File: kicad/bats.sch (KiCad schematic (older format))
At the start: 12 parts

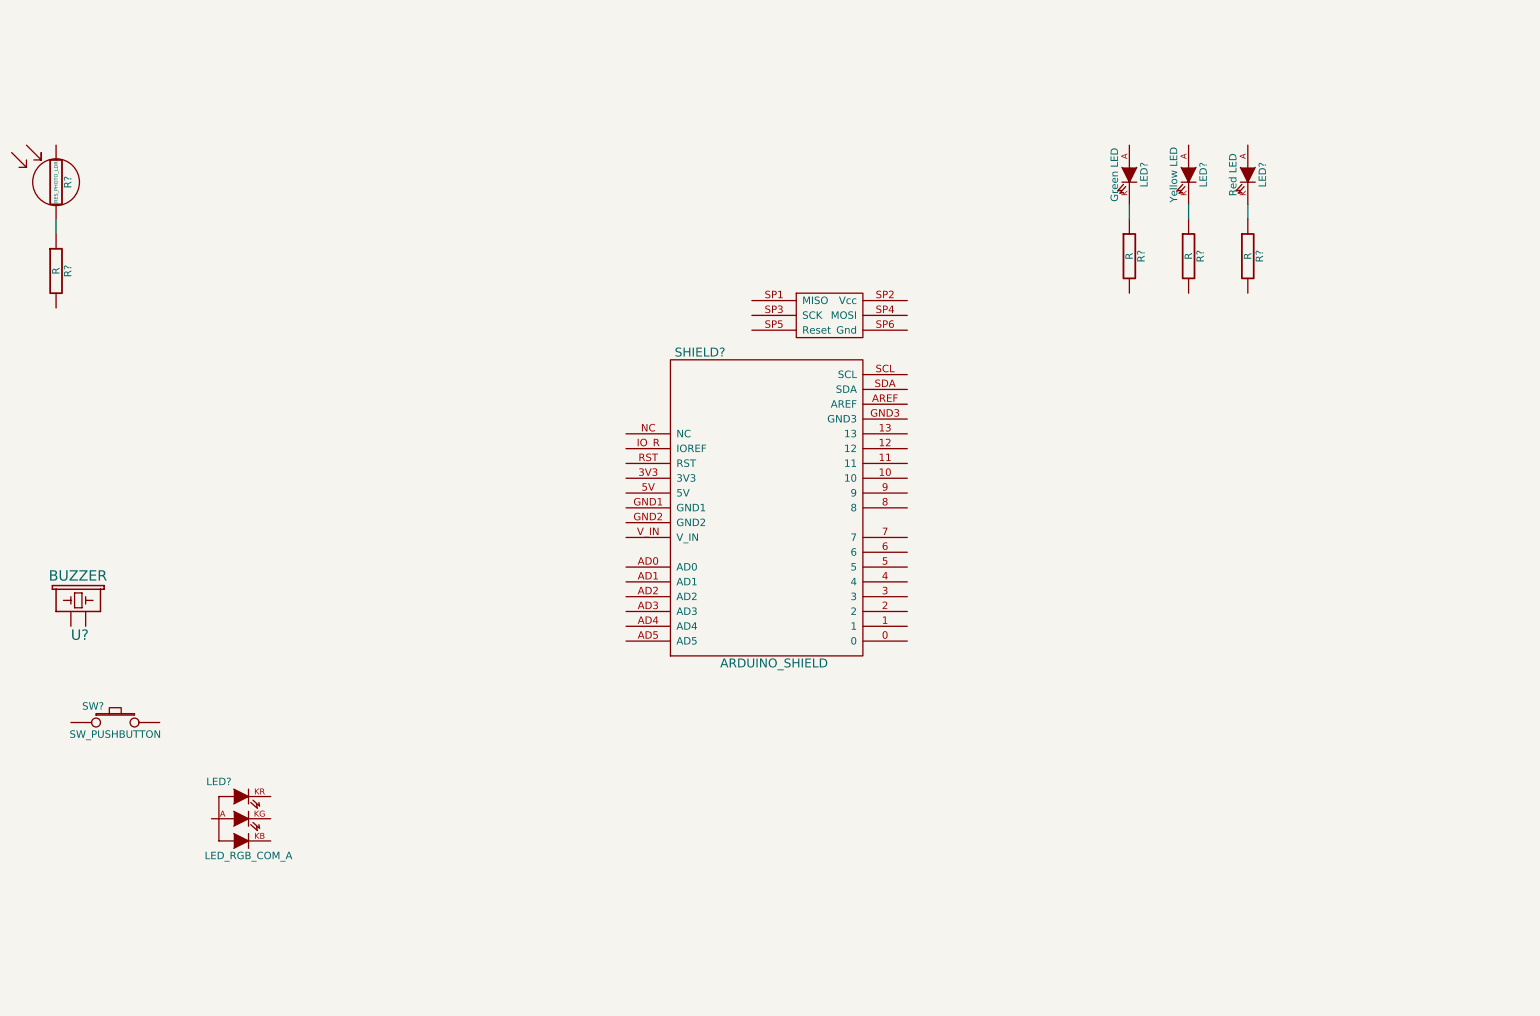
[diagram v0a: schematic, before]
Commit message: Mais avances no esquema do circuito
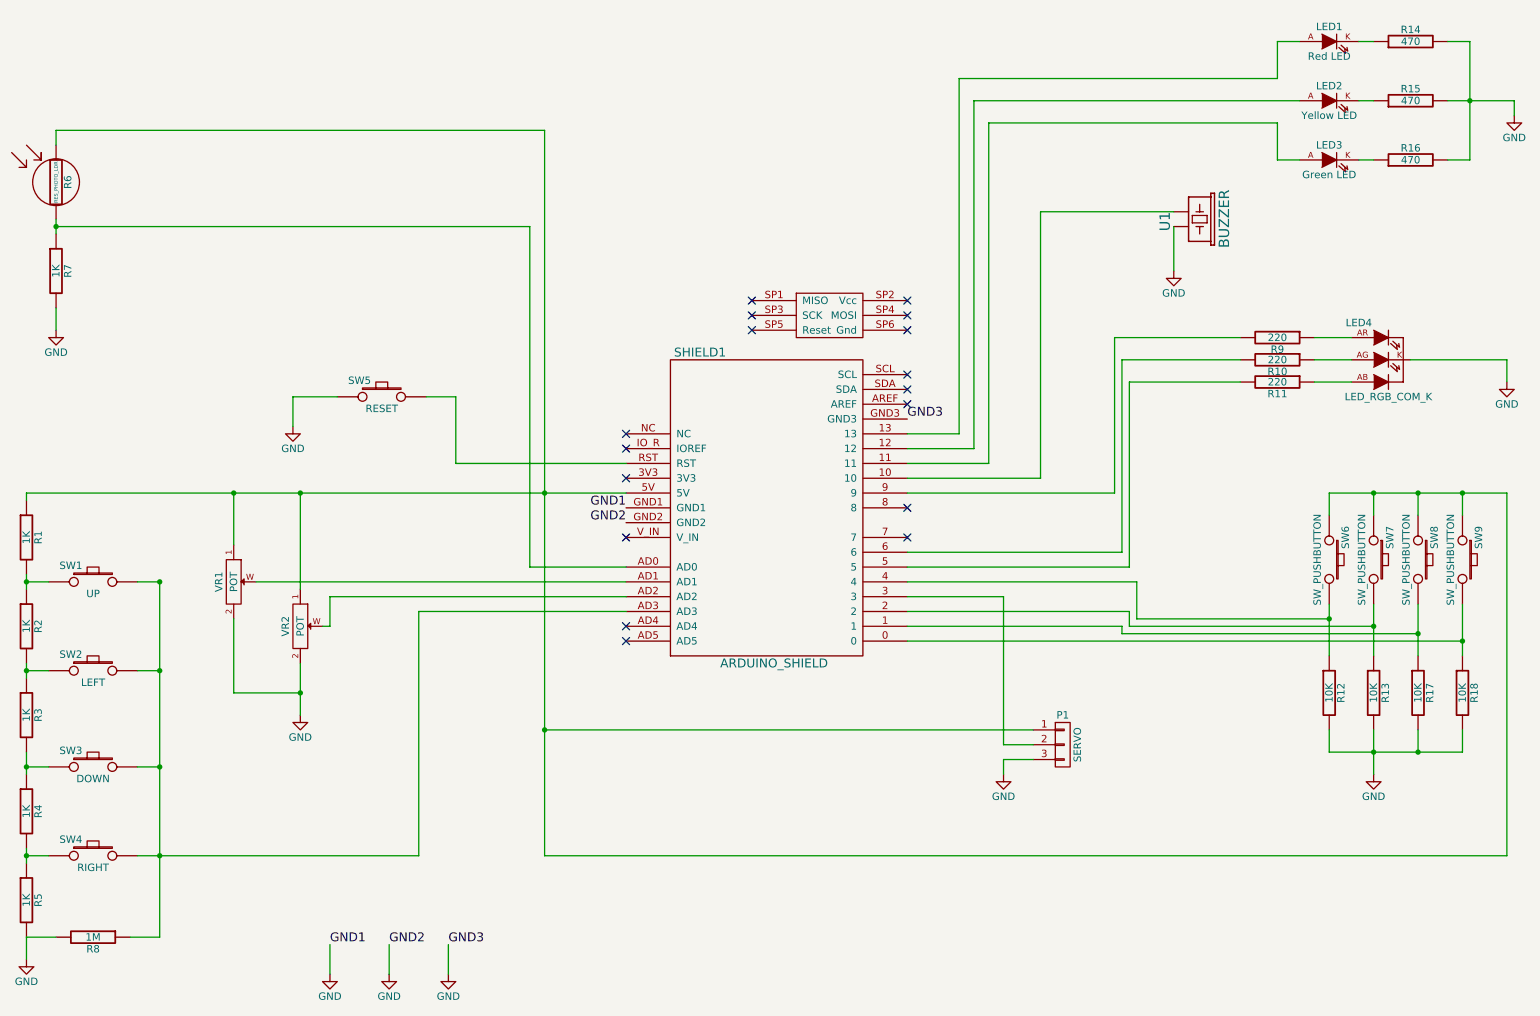
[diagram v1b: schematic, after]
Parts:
- removed LED?: LED_RGB_COM_A, symbol LED_RGB_COM_A
- added LED4: LED_RGB_COM_K, FT:LED_CUBE_BASE_4PIN, symbol LED_RGB_COM_K
- added P1: SERVO, FT:1X03, symbol CONN_01X03
- added R1, R2, R3, R4, R5: 1K, Resistors_ThroughHole:Resistor_Horizontal_RM10mm, symbol R
- added R10, R11, R9: 220, Resistors_ThroughHole:Resistor_Horizontal_RM10mm, symbol R
- added R12, R13, R17, R18: 10K, Resistors_ThroughHole:Resistor_Horizontal_RM10mm, symbol R
- added R8: 1M, Resistors_ThroughHole:Resistor_Horizontal_RM10mm, symbol R
- added SW1: UP, FT:SW_PUSHBUTTON_PTH, symbol SW_PUSHBUTTON
- added SW2: LEFT, FT:SW_PUSHBUTTON_PTH, symbol SW_PUSHBUTTON
- added SW3: DOWN, FT:SW_PUSHBUTTON_PTH, symbol SW_PUSHBUTTON
- added SW4: RIGHT, FT:SW_PUSHBUTTON_PTH, symbol SW_PUSHBUTTON
- added SW5: RESET, FT:SW_PUSHBUTTON_PTH, symbol SW_PUSHBUTTON
- added SW7, SW8: SW_PUSHBUTTON, FT:SW_PUSHBUTTON_PTH, symbol SW_PUSHBUTTON
- added SW9: SW_PUSHBUTTON, Buttons_Switches_ThroughHole:SW_PUSH, symbol SW_PUSHBUTTON
- added VR1, VR2: POT, Potentiometers:Potentiometer_Alps-RK16-single, symbol POT
- LED1, LED2, LED3: renamed from LED?; footprint (none) -> FT:LED-3MM
- R14, R15, R16: renamed from R?; value R -> 470; footprint (none) -> Resistors_ThroughHole:Resistor_Horizontal_RM10mm
- R6: renamed from R?; footprint (none) -> Resistors_ThroughHole:Resistor_Horizontal_RM10mm
- R7: renamed from R?; value R -> 1K; footprint (none) -> Resistors_ThroughHole:Resistor_Horizontal_RM10mm
- SW6: renamed from SW?; footprint (none) -> FT:SW_PUSHBUTTON_PTH
- U1: renamed from U?; footprint (none) -> Buzzers_Beepers:MagneticBuzzer_StarMicronics_HMB-06_HMB-12
- gave numbers to parts that had none: 1
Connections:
- net at SHIELD1.0: now also R18.1, SW9.2
- net at SHIELD1.1: now also R17.1, SW8.2
- net at SHIELD1.10: now also U1.2 (GND)
- net at SHIELD1.11: now also LED3.A
- net at SHIELD1.12: now also LED2.A
- net at SHIELD1.13: now also LED1.A
- net at SHIELD1.2: now also R13.1, SW7.2
- net at SHIELD1.3: now also P1.2 (P2)
- net at SHIELD1.4: now also SW6.2, R12.1
- net at SHIELD1.5: now also R11.2
- net at SHIELD1.5V: now also R6.1, SW6.1, P1.1 (P1), R1.1, SW7.1, SW8.1, SW9.1, VR1.1, VR2.1
- net at SHIELD1.6: now also R10.2
- net at SHIELD1.9: now also R9.2
- net at SHIELD1.AD0: now also R6.2, R7.1
- net at SHIELD1.AD1: now also VR1.W
- net at SHIELD1.AD2: now also VR2.W
- net at SHIELD1.AD3: now also R8.1, SW1.2, SW2.2, SW3.2, SW4.2
- net GND: now reaches SHIELD1.GND1
- net GND: now also R14.2, R15.2, R16.2, R7.2, SHIELD1.GND2, SHIELD1.GND3, U1.1 (POS), LED4.K, P1.3 (P3), R12.2, R13.2, R17.2, R18.2, R5.2, R8.2, SW5.1, VR1.2, VR2.2
- net at SHIELD1.RST: now also SW5.2
- new net: LED4.AB, R11.1
- new net: LED4.AG, R10.1
- new net: LED4.AR, R9.1
- new net: R1.2, R2.1, SW1.1
- new net: R2.2, R3.1, SW2.1
- new net: R3.2, R4.1, SW3.1
- new net: R4.2, R5.1, SW4.1
- no-connect marks 0 -> 17
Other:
- moved on the sheet: LED1, LED2, LED3, R14, R15, R16, SW6, U1

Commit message: Engadido o esquema en formato pdf
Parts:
- SW6: value SW_PUSHBUTTON -> UP
- SW7: value SW_PUSHBUTTON -> LEFT
- SW8: value SW_PUSHBUTTON -> DOWN
- SW9: value SW_PUSHBUTTON -> RIGHT
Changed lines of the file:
@@
 P 9600 4300
 F 0 "SW6" H 9450 4410 50  0000 C CNN
-F 1 "SW_PUSHBUTTON" H 9600 4220 50  0000 C CNN
+F 1 "UP" H 9600 4220 50  0000 C CNN
 F 2 "FT:SW_PUSHBUTTON_PTH" H 9600 4300 60  0001 C CNN
 F 3 "" H 9600 4300 60  0000 C CNN
@@
 P 9900 4300
 F 0 "SW7" H 9750 4410 50  0000 C CNN
-F 1 "SW_PUSHBUTTON" H 9900 4220 50  0000 C CNN
+F 1 "LEFT" H 9900 4220 50  0000 C CNN
 F 2 "FT:SW_PUSHBUTTON_PTH" H 9900 4300 60  0001 C CNN
 F 3 "" H 9900 4300 60  0000 C CNN
@@
 P 10200 4300
 F 0 "SW8" H 10050 4410 50  0000 C CNN
-F 1 "SW_PUSHBUTTON" H 10200 4220 50  0000 C CNN
+F 1 "DOWN" H 10200 4220 50  0000 C CNN
 F 2 "FT:SW_PUSHBUTTON_PTH" H 10200 4300 60  0001 C CNN
 F 3 "" H 10200 4300 60  0000 C CNN
@@
 P 10500 4300
 F 0 "SW9" H 10350 4410 50  0000 C CNN
-F 1 "SW_PUSHBUTTON" H 10500 4220 50  0000 C CNN
+F 1 "RIGHT" H 10500 4220 50  0000 C CNN
 F 2 "Buttons_Switches_ThroughHole:SW_PUSH" H 10500 4300 60  0001 C CNN
 F 3 "" H 10500 4300 60  0000 C CNN
@@
 	9900 800  9800 800
 Wire Wire Line
-	1000 2000 1000 2100
+	1000 2000 1000 2050
+Wire Wire Line
+	1000 2050 1000 2100
 Wire Wire Line
 	10550 1600 10400 1600
 Wire Wire Line
-	10550 800  10550 1600
+	10550 800  10550 1200
+Wire Wire Line
+	10550 1200 10550 1600
 Wire Wire Line
 	10550 800  10400 800
 Wire Wire Line
-	10400 1200 10850 1200
+	10400 1200 10550 1200
+Wire Wire Line
+	10550 1200 10850 1200
 Connection ~ 10550 1200
 Wire Wire Line
@@
 Connection ~ 1000 2050
 Wire Wire Line
-	800  3850 4850 3850
-Wire Wire Line
-	4300 1400 4300 6300
+	800  3850 2200 3850
+Wire Wire Line
+	2200 3850 2650 3850
+Wire Wire Line
+	2650 3850 4300 3850
+Wire Wire Line
+	4300 3850 4850 3850
+Wire Wire Line
+	4300 1400 4300 3850
+Wire Wire Line
+	4300 3850 4300 5450
+Wire Wire Line
+	4300 5450 4300 6300
 Wire Wire Line
 	4300 1400 1000 1400
@@
 	8550 2050 8550 2350
 Wire Wire Line
-	9600 4600 9600 4950
-Wire Wire Line
-	9900 4600 9900 4950
-Wire Wire Line
-	10200 4600 10200 4950
-Wire Wire Line
-	10500 4600 10500 4950
+	9600 4600 9600 4700
+Wire Wire Line
+	9600 4700 9600 4950
+Wire Wire Line
+	9900 4600 9900 4750
+Wire Wire Line
+	9900 4750 9900 4950
+Wire Wire Line
+	10200 4600 10200 4800
+Wire Wire Line
+	10200 4800 10200 4950
+Wire Wire Line
+	10500 4600 10500 4850
+Wire Wire Line
+	10500 4850 10500 4950
 Wire Wire Line
 	9900 3850 9900 4000
@@
 Connection ~ 10500 3850
 Wire Wire Line
-	9600 3850 10800 3850
+	9600 3850 9900 3850
+Wire Wire Line
+	9900 3850 10200 3850
+Wire Wire Line
+	10200 3850 10500 3850
+Wire Wire Line
+	10500 3850 10800 3850
 Wire Wire Line
 	9600 3850 9600 4000
@@
 	9600 5450 9600 5600
 Wire Wire Line
-	9600 5600 10500 5600
+	9600 5600 9900 5600
+Wire Wire Line
+	9900 5600 10200 5600
+Wire Wire Line
+	10200 5600 10500 5600
 Wire Wire Line
 	10500 5600 10500 5450
 Wire Wire Line
-	9900 5450 9900 5750
+	9900 5450 9900 5600
+Wire Wire Line
+	9900 5600 9900 5750
 Connection ~ 9900 5600
 Wire Wire Line
@@
 	7400 5650 7400 5750
 Wire Wire Line
-	1700 4450 1700 6850
+	1700 4450 1700 5050
+Wire Wire Line
+	1700 5050 1700 5700
+Wire Wire Line
+	1700 5700 1700 6300
+Wire Wire Line
+	1700 6300 1700 6850
 Wire Wire Line
 	1550 5700 1700 5700
@@
 Connection ~ 1700 5050
 Wire Wire Line
-	800  4400 800  4500
+	800  4400 800  4450
+Wire Wire Line
+	800  4450 800  4500
 Wire Wire Line
 	950  4450 800  4450
 Connection ~ 800  4450
 Wire Wire Line
-	800  5000 800  5100
+	800  5000 800  5050
+Wire Wire Line
+	800  5050 800  5100
 Wire Wire Line
 	950  5050 800  5050
 Connection ~ 800  5050
 Wire Wire Line
-	800  5600 800  5750
+	800  5600 800  5700
+Wire Wire Line
+	800  5700 800  5750
 Wire Wire Line
 	950  5700 800  5700
 Connection ~ 800  5700
 Wire Wire Line
-	800  6250 800  6350
+	800  6250 800  6300
+Wire Wire Line
+	800  6300 800  6350
 Wire Wire Line
 	950  6300 800  6300
@@
 	1700 6850 1500 6850
 Wire Wire Line
-	1550 6300 3450 6300
+	1550 6300 1700 6300
+Wire Wire Line
+	1700 6300 3450 6300
 Connection ~ 1700 6300
 Wire Wire Line
@@
 	2200 5200 2650 5200
 Wire Wire Line
-	2650 5000 2650 5350
+	2650 5000 2650 5200
+Wire Wire Line
+	2650 5200 2650 5350
 Connection ~ 2650 5200
 Wire Wire Line

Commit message: A PCB empeza a coller forma.
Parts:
- LED4: footprint FT:LED_CUBE_BASE_4PIN -> FT:LED-RGB-8MM-COM-K-MINIMAL
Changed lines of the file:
@@
 F 0 "LED4" H 9800 2900 50  0000 C CNN
 F 1 "LED_RGB_COM_K" H 10000 2400 50  0000 C CNN
-F 2 "FT:LED_CUBE_BASE_4PIN" H 9950 2800 60  0001 C CNN
+F 2 "FT:LED-RGB-8MM-COM-K-MINIMAL" H 9950 2800 60  0001 C CNN
 F 3 "" H 9950 2800 60  0000 C CNN
 	1    9950 2800
@@
 	9900 800  9800 800
 Wire Wire Line
-	1000 2000 1000 2050
-Wire Wire Line
-	1000 2050 1000 2100
+	1000 2000 1000 2100
 Wire Wire Line
 	10550 1600 10400 1600
 Wire Wire Line
-	10550 800  10550 1200
-Wire Wire Line
-	10550 1200 10550 1600
+	10550 800  10550 1600
 Wire Wire Line
 	10550 800  10400 800
 Wire Wire Line
-	10400 1200 10550 1200
-Wire Wire Line
-	10550 1200 10850 1200
+	10400 1200 10850 1200
 Connection ~ 10550 1200
 Wire Wire Line
@@
 Connection ~ 1000 2050
 Wire Wire Line
-	800  3850 2200 3850
-Wire Wire Line
-	2200 3850 2650 3850
-Wire Wire Line
-	2650 3850 4300 3850
-Wire Wire Line
-	4300 3850 4850 3850
-Wire Wire Line
-	4300 1400 4300 3850
-Wire Wire Line
-	4300 3850 4300 5450
-Wire Wire Line
-	4300 5450 4300 6300
+	800  3850 4850 3850
+Wire Wire Line
+	4300 1400 4300 6300
 Wire Wire Line
 	4300 1400 1000 1400
@@
 	8550 2050 8550 2350
 Wire Wire Line
-	9600 4600 9600 4700
-Wire Wire Line
-	9600 4700 9600 4950
-Wire Wire Line
-	9900 4600 9900 4750
-Wire Wire Line
-	9900 4750 9900 4950
-Wire Wire Line
-	10200 4600 10200 4800
-Wire Wire Line
-	10200 4800 10200 4950
-Wire Wire Line
-	10500 4600 10500 4850
-Wire Wire Line
-	10500 4850 10500 4950
+	9600 4600 9600 4950
+Wire Wire Line
+	9900 4600 9900 4950
+Wire Wire Line
+	10200 4600 10200 4950
+Wire Wire Line
+	10500 4600 10500 4950
 Wire Wire Line
 	9900 3850 9900 4000
@@
 Connection ~ 10500 3850
 Wire Wire Line
-	9600 3850 9900 3850
-Wire Wire Line
-	9900 3850 10200 3850
-Wire Wire Line
-	10200 3850 10500 3850
-Wire Wire Line
-	10500 3850 10800 3850
+	9600 3850 10800 3850
 Wire Wire Line
 	9600 3850 9600 4000
@@
 	9600 5450 9600 5600
 Wire Wire Line
-	9600 5600 9900 5600
-Wire Wire Line
-	9900 5600 10200 5600
-Wire Wire Line
-	10200 5600 10500 5600
+	9600 5600 10500 5600
 Wire Wire Line
 	10500 5600 10500 5450
 Wire Wire Line
-	9900 5450 9900 5600
-Wire Wire Line
-	9900 5600 9900 5750
+	9900 5450 9900 5750
 Connection ~ 9900 5600
 Wire Wire Line
@@
 	7400 5650 7400 5750
 Wire Wire Line
-	1700 4450 1700 5050
-Wire Wire Line
-	1700 5050 1700 5700
-Wire Wire Line
-	1700 5700 1700 6300
-Wire Wire Line
-	1700 6300 1700 6850
+	1700 4450 1700 6850
 Wire Wire Line
 	1550 5700 1700 5700
@@
 Connection ~ 1700 5050
 Wire Wire Line
-	800  4400 800  4450
-Wire Wire Line
-	800  4450 800  4500
+	800  4400 800  4500
 Wire Wire Line
 	950  4450 800  4450
 Connection ~ 800  4450
 Wire Wire Line
-	800  5000 800  5050
-Wire Wire Line
-	800  5050 800  5100
+	800  5000 800  5100
 Wire Wire Line
 	950  5050 800  5050
 Connection ~ 800  5050
 Wire Wire Line
-	800  5600 800  5700
-Wire Wire Line
-	800  5700 800  5750
+	800  5600 800  5750
 Wire Wire Line
 	950  5700 800  5700
 Connection ~ 800  5700
 Wire Wire Line
-	800  6250 800  6300
-Wire Wire Line
-	800  6300 800  6350
+	800  6250 800  6350
 Wire Wire Line
 	950  6300 800  6300
@@
 	1700 6850 1500 6850
 Wire Wire Line
-	1550 6300 1700 6300
-Wire Wire Line
-	1700 6300 3450 6300
+	1550 6300 3450 6300
 Connection ~ 1700 6300
 Wire Wire Line
@@
 	2200 5200 2650 5200
 Wire Wire Line
-	2650 5000 2650 5200
-Wire Wire Line
-	2650 5200 2650 5350
+	2650 5000 2650 5350
 Connection ~ 2650 5200
 Wire Wire Line

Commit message: Mais cambios non especificados, facemos o commit antes de borrar o conxunto de pulsadores analóxicos.
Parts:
- SW9: footprint Buttons_Switches_ThroughHole:SW_PUSH -> FT:SW_PUSHBUTTON_PTH
- VR1, VR2: footprint Potentiometers:Potentiometer_Alps-RK16-single -> (none)
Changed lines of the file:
@@
 $EndComp
 $Comp
-L GND #PWR01
+L GND #PWR2
 U 1 1 558AD005
 P 1000 2750
-F 0 "#PWR01" H 1000 2500 50  0001 C CNN
+F 0 "#PWR2" H 1000 2500 50  0001 C CNN
 F 1 "GND" H 1000 2600 50  0000 C CNN
 F 2 "" H 1000 2750 60  0000 C CNN
@@
 $EndComp
 $Comp
-L GND #PWR02
+L GND #PWR9
 U 1 1 558AE0E5
 P 8550 2350
-F 0 "#PWR02" H 8550 2100 50  0001 C CNN
+F 0 "#PWR9" H 8550 2100 50  0001 C CNN
 F 1 "GND" H 8550 2200 50  0000 C CNN
 F 2 "" H 8550 2350 60  0000 C CNN
@@
 F 0 "SW9" H 10350 4410 50  0000 C CNN
 F 1 "RIGHT" H 10500 4220 50  0000 C CNN
-F 2 "Buttons_Switches_ThroughHole:SW_PUSH" H 10500 4300 60  0001 C CNN
+F 2 "FT:SW_PUSHBUTTON_PTH" H 10500 4300 60  0001 C CNN
 F 3 "" H 10500 4300 60  0000 C CNN
 	1    10500 4300
@@
 $EndComp
 $Comp
-L GND #PWR03
+L GND #PWR10
 U 1 1 558AF401
 P 9900 5750
-F 0 "#PWR03" H 9900 5500 50  0001 C CNN
+F 0 "#PWR10" H 9900 5500 50  0001 C CNN
 F 1 "GND" H 9900 5600 50  0000 C CNN
 F 2 "" H 9900 5750 60  0000 C CNN
@@
 $EndComp
 $Comp
-L GND #PWR04
+L GND #PWR11
 U 1 1 558B19E1
 P 10800 3100
-F 0 "#PWR04" H 10800 2850 50  0001 C CNN
+F 0 "#PWR11" H 10800 2850 50  0001 C CNN
 F 1 "GND" H 10800 2950 50  0000 C CNN
 F 2 "" H 10800 3100 60  0000 C CNN
@@
 $EndComp
 $Comp
-L GND #PWR05
+L GND #PWR8
 U 1 1 558B2CF4
 P 7400 5750
-F 0 "#PWR05" H 7400 5500 50  0001 C CNN
+F 0 "#PWR8" H 7400 5500 50  0001 C CNN
 F 1 "GND" H 7400 5600 50  0000 C CNN
 F 2 "" H 7400 5750 60  0000 C CNN
@@
 $EndComp
 $Comp
-L GND #PWR06
+L GND #PWR1
 U 1 1 558B5809
 P 800 7000
-F 0 "#PWR06" H 800 6750 50  0001 C CNN
+F 0 "#PWR1" H 800 6750 50  0001 C CNN
 F 1 "GND" H 800 6850 50  0000 C CNN
 F 2 "" H 800 7000 60  0000 C CNN
@@
 $EndComp
 $Comp
-L POT VR1
-U 1 1 558B64D3
-P 2200 4450
-F 0 "VR1" H 2200 4350 50  0000 C CNN
-F 1 "POT" H 2200 4450 50  0000 C CNN
-F 2 "Potentiometers:Potentiometer_Alps-RK16-single" H 2200 4450 60  0001 C CNN
-F 3 "" H 2200 4450 60  0000 C CNN
-	1    2200 4450
-	0    1    1    0
-$EndComp
-$Comp
-L POT VR2
-U 1 1 558B673E
-P 2650 4750
-F 0 "VR2" H 2650 4650 50  0000 C CNN
-F 1 "POT" H 2650 4750 50  0000 C CNN
-F 2 "Potentiometers:Potentiometer_Alps-RK16-single" H 2650 4750 60  0001 C CNN
-F 3 "" H 2650 4750 60  0000 C CNN
-	1    2650 4750
-	0    1    1    0
-$EndComp
-$Comp
-L GND #PWR07
+L GND #PWR4
 U 1 1 558B6A63
 P 2650 5350
-F 0 "#PWR07" H 2650 5100 50  0001 C CNN
+F 0 "#PWR4" H 2650 5100 50  0001 C CNN
 F 1 "GND" H 2650 5200 50  0000 C CNN
 F 2 "" H 2650 5350 60  0000 C CNN
@@
 $EndComp
 $Comp
-L GND #PWR08
+L GND #PWR3
 U 1 1 558B7665
 P 2600 3400
-F 0 "#PWR08" H 2600 3150 50  0001 C CNN
+F 0 "#PWR3" H 2600 3150 50  0001 C CNN
 F 1 "GND" H 2600 3250 50  0000 C CNN
 F 2 "" H 2600 3400 60  0000 C CNN
@@
 	2600 3200 2600 3400
 $Comp
-L GND #PWR09
+L GND #PWR12
 U 1 1 558C0B72
 P 10850 1300
-F 0 "#PWR09" H 10850 1050 50  0001 C CNN
+F 0 "#PWR12" H 10850 1050 50  0001 C CNN
 F 1 "GND" H 10850 1150 50  0000 C CNN
 F 2 "" H 10850 1300 60  0000 C CNN
@@
 GND1
 $Comp
-L GND #PWR010
+L GND #PWR5
 U 1 1 558C28FA
 P 2850 7100
-F 0 "#PWR010" H 2850 6850 50  0001 C CNN
+F 0 "#PWR5" H 2850 6850 50  0001 C CNN
 F 1 "GND" H 2850 6950 50  0000 C CNN
 F 2 "" H 2850 7100 60  0000 C CNN
@@
 GND2
 $Comp
-L GND #PWR011
+L GND #PWR6
 U 1 1 558C3402
 P 3250 7100
-F 0 "#PWR011" H 3250 6850 50  0001 C CNN
+F 0 "#PWR6" H 3250 6850 50  0001 C CNN
 F 1 "GND" H 3250 6950 50  0000 C CNN
 F 2 "" H 3250 7100 60  0000 C CNN
@@
 	2850 4750 2800 4750
 $Comp
-L GND #PWR012
+L GND #PWR7
 U 1 1 558C5111
 P 3650 7100
-F 0 "#PWR012" H 3650 6850 50  0001 C CNN
+F 0 "#PWR7" H 3650 6850 50  0001 C CNN
 F 1 "GND" H 3650 6950 50  0000 C CNN
 F 2 "" H 3650 7100 60  0000 C CNN
@@
 Text Label 6750 3350 0    60   ~ 0
 GND3
+$Comp
+L POT VR1
+U 1 1 558C95A2
+P 2200 4450
+F 0 "VR1" H 2200 4350 50  0000 C CNN
+F 1 "POT" H 2200 4450 50  0000 C CNN
+F 2 "" H 2200 4450 60  0000 C CNN
+F 3 "" H 2200 4450 60  0000 C CNN
+	1    2200 4450
+	0    1    1    0
+$EndComp
+$Comp
+L POT VR2
+U 1 1 558C972F
+P 2650 4750
+F 0 "VR2" H 2650 4650 50  0000 C CNN
+F 1 "POT" H 2650 4750 50  0000 C CNN
+F 2 "" H 2650 4750 60  0000 C CNN
+F 3 "" H 2650 4750 60  0000 C CNN
+	1    2650 4750
+	0    1    1    0
+$EndComp
 $EndSCHEMATC
